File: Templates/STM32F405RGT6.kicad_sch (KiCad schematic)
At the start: 28 parts, among them J1 USB_B_Micro, J2 Conn_01x04_Pin, SW1 SW_SPDT, U1 STM32F405RGTx, U2 AMS1117-3.3, Y1 16MHz

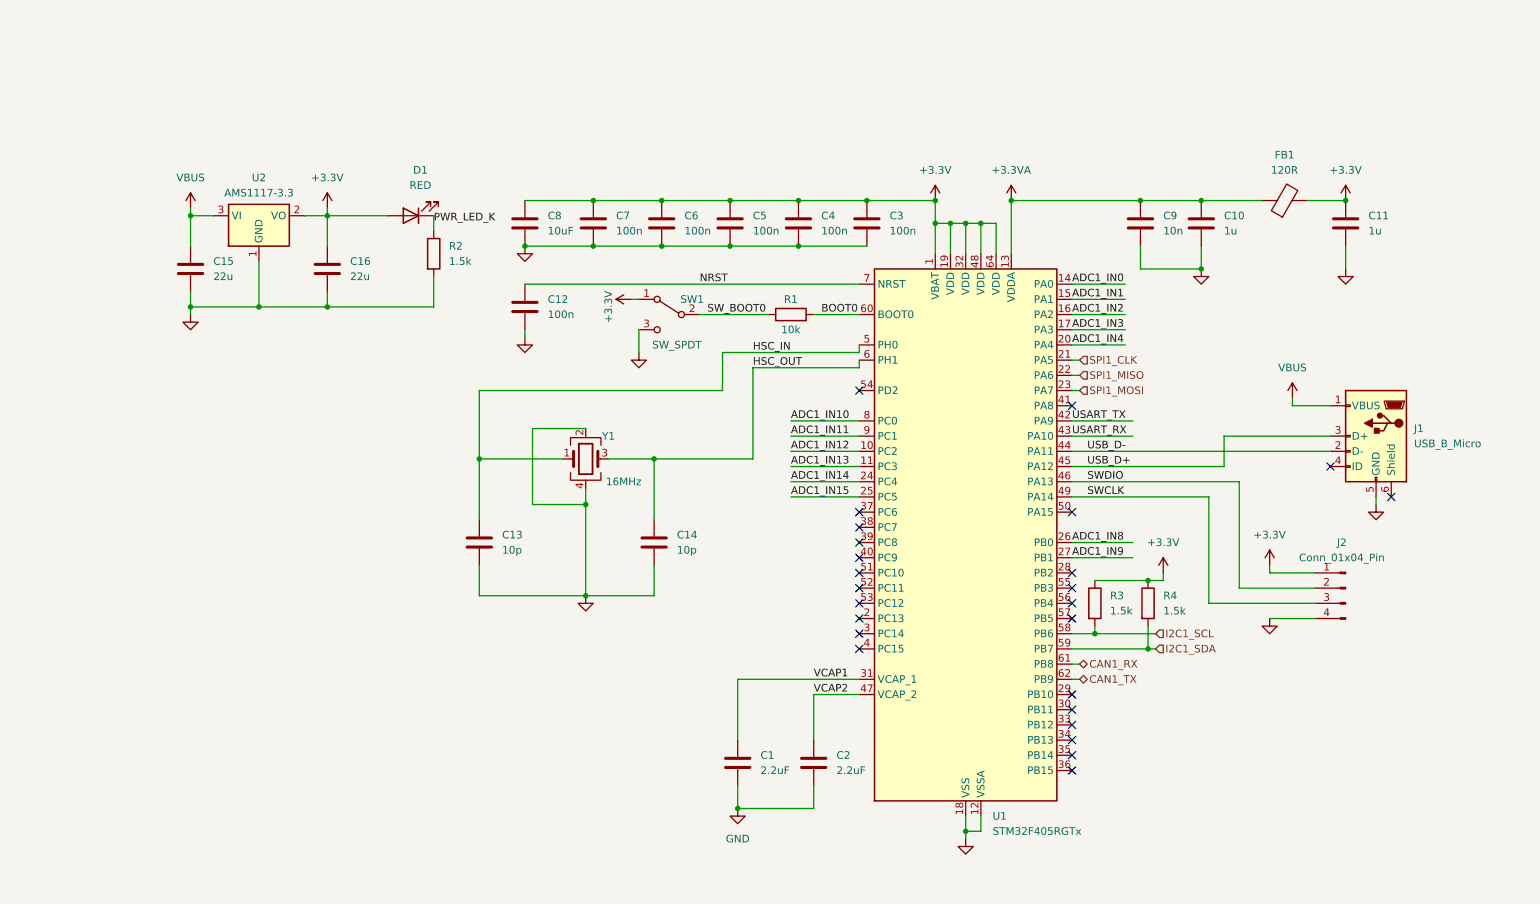
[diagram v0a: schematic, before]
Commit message: Updated STM32F405RGT6 template
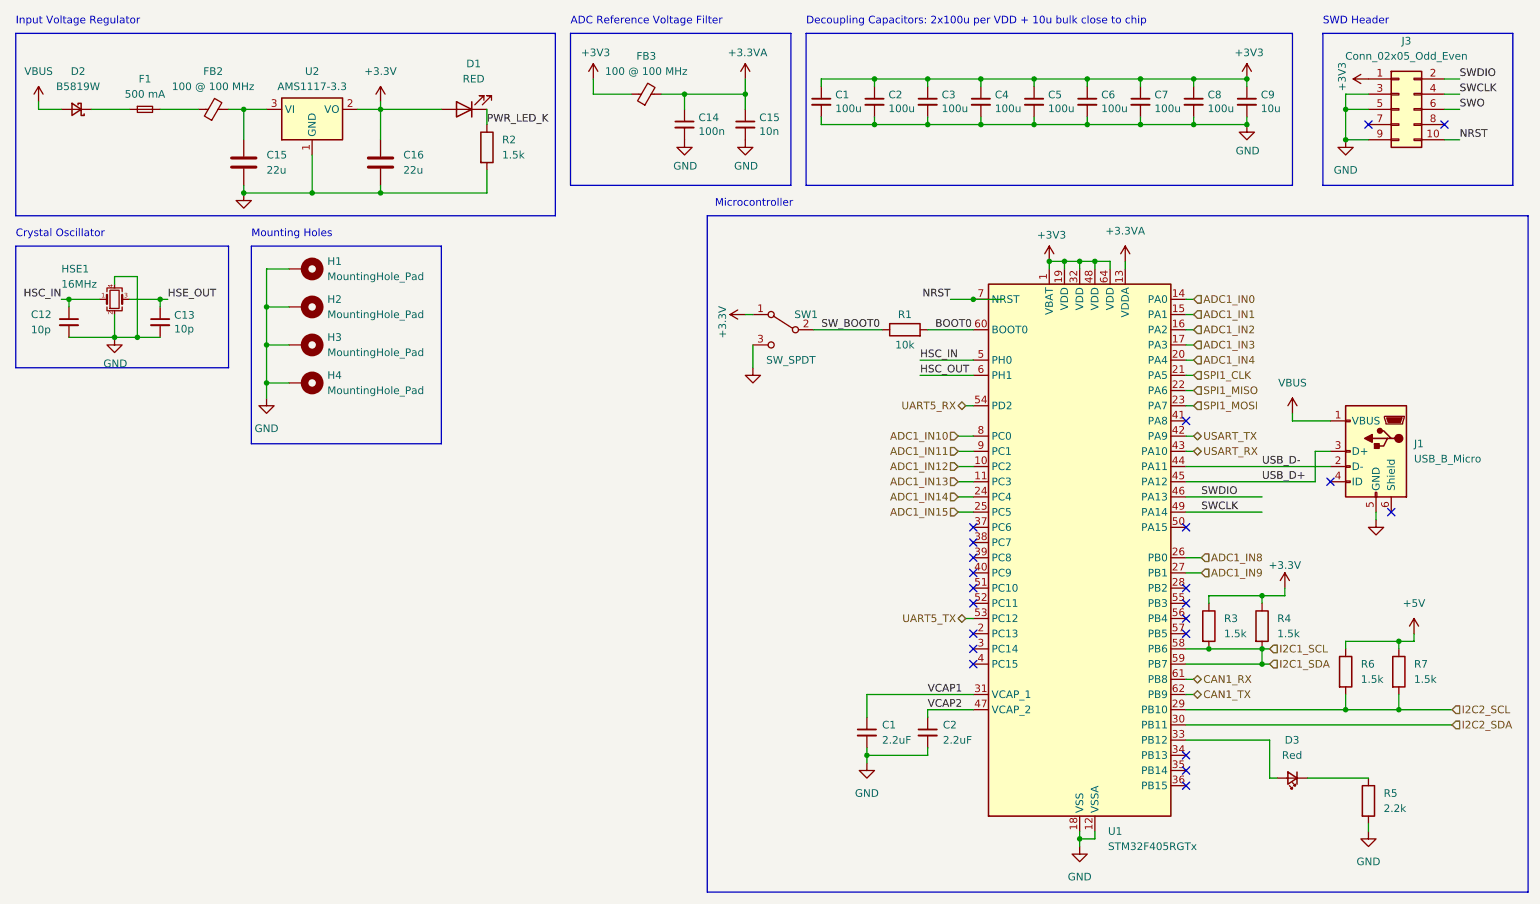
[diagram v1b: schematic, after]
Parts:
- removed C1, C2: 2.2uF, symbol Device:C
- removed C10, C11: 1u, symbol Device:C
- removed C12, C3, C4, C5, C6, C7: 100n, symbol Device:C
- removed C13, C14: 10p, symbol Device:C
- removed C8: 10uF, symbol Device:C
- removed C9: 10n, symbol Device:C
- removed FB1: 120R, symbol Device:FerriteBead
- removed J2: Conn_01x04_Pin, symbol Connector:Conn_01x04_Pin
- removed Y1: 16MHz, symbol Device:Crystal_GND24
- added C1, C2, C3, C4, C5, C6, C7, C8: 100u, Capacitor_SMD:C_0402_1005Metric, symbol Device:C_Small
- added C1, C2: 2.2uF, symbol Device:C_Small
- added C12, C13: 10p, Capacitor_SMD:C_0402_1005Metric, symbol Device:C_Small
- added C14: 100n, Capacitor_SMD:C_0402_1005Metric, symbol Device:C_Small
- added C15: 10n, Capacitor_SMD:C_0402_1005Metric, symbol Device:C_Small
- added C9: 10u, Capacitor_SMD:C_0603_1608Metric, symbol Device:C_Small
- added D2: B5819W, symbol Device:D_Schottky_Small
- added D3: Red, symbol Device:LED_Small
- added F1: 500 mA, symbol Device:Fuse_Small
- added FB2, FB3: 100 @ 100 MHz, symbol Device:FerriteBead_Small
- added H1, H2, H3, H4: MountingHole_Pad, symbol Mechanical:MountingHole_Pad
- added HSE1: 16MHz, Crystal:Crystal_SMD_3225-4Pin_3.2x2.5mm, symbol Device:Crystal_GND24_Small
- added J3: Conn_02x05_Odd_Even, symbol Connector_Generic:Conn_02x05_Odd_Even
- added R5: 2.2k, symbol Device:R
- added R6, R7: 1.5k, symbol Device:R
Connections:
- net I2C1_SDA is gone; now on net I2C1_SCL: R4.2, U1.59 (PB7)
- net +3.3V: no longer U1.1 (VBAT), U1.19 (VDD), U1.32 (VDD), U1.48 (VDD), U1.64 (VDD)
- net +3.3VA: now also C14.1, C15.1, FB3.2
- net GND: now also C1.2, C1.2, C12.2, C13.2, C14.2, C15.2, C2.2, C2.2, C3.2, C4.2, C5.2, C6.2, C7.2, C8.2, C9.2, H1.1, H2.1, H3.1, H4.1, HSE1.2, HSE1.4, J3.3 (Pin_3), J3.5 (Pin_5), J3.9 (Pin_9), R5.2
- net HSC_IN: now also C12.1, HSE1.1
- net NRST: now also J3.10 (Pin_10)
- net SWCLK: now also J3.4 (Pin_4)
- net SWDIO: now also J3.2 (Pin_2)
- net VBUS: now also D2.2 (A); no longer C15.1, U2.3 (VI)
- net VCAP1: now also C1.1
- net VCAP2: now also C2.1
- net I2C2_SCL: now reaches U1.29 (PB10)
- net I2C2_SCL: now also R6.2, R7.2
- net I2C2_SDA: now reaches U1.30 (PB11)
- net at U1.33 (PB12): now also D3.2 (A)
- net UART5_TX: now reaches U1.53 (PC12)
- net UART5_RX: now reaches U1.54 (PD2)
- new net: F1.2, FB2.1
- new net: C15.1, FB2.2, U2.3 (VI)
- new net: D2.1 (K), F1.1
- new net: D3.1 (K), R5.1
- new net +3V3: C1.1, C2.1, C3.1, C4.1, C5.1, C6.1, C7.1, C8.1, C9.1, FB3.1, J3.1 (Pin_1), U1.1 (VBAT), U1.19 (VDD), U1.32 (VDD), U1.48 (VDD), U1.64 (VDD)
- new net +5V: R6.1, R7.1
- new net HSE_OUT: C13.1, HSE1.3
- new net SWO: J3.6 (Pin_6)
- no-connect marks 25 -> 22
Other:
- note added: "ADC Reference Voltage Filter"
- note added: "Crystal Oscillator"
- note added: "Decoupling Capacitors: 2x100u per VDD + 10u bulk close to chip"
- note added: "Input Voltage Regulator"
- note added: "Microcontroller"
- note added: "Mounting Holes"
- note added: "SWD Header"
- moved on the sheet: C15, C16, D1, J1, R1, R2, R3, R4, SW1, U1, U2
